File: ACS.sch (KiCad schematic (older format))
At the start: 30 parts, among them J1 5v? Igniter power source, J2 RJ45, J3 RJ45, P1 CONN_01X02, P10 ABT TOG, P11 LOX MPV, P12 LNCH SFT, P13 LNCH TOG, P14 CH4 MPV, P15 LOX VNT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

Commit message: Added version number
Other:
- note added: "Version: 4.10.18"
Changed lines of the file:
@@
 LIBS:power
 LIBS:device
+LIBS:switches
+LIBS:relays
+LIBS:motors
 LIBS:transistors
 LIBS:conn
@@
 	1750 3700 1750 5500
 NoConn ~ 1600 3550
+Text Notes 4550 5750 0    60   ~ 0
+Version: 4.10.18
 $EndSCHEMATC

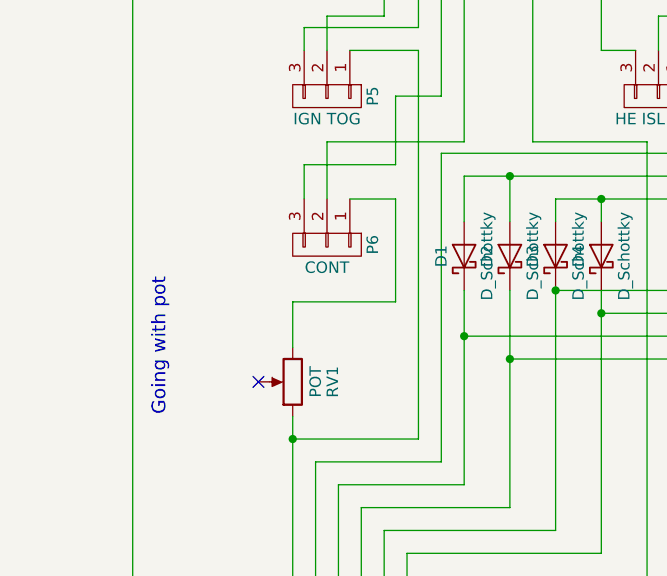
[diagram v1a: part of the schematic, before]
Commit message: Trimmer Resistor, finished circuit
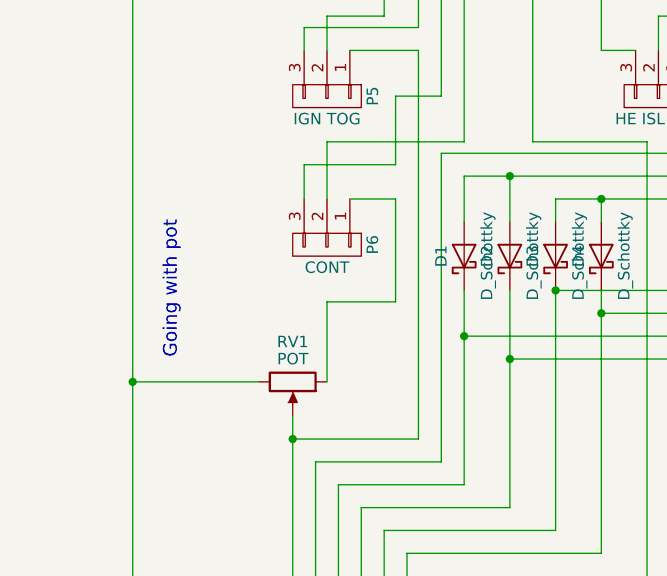
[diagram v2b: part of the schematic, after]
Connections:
- net at J2.1, P1.2 (P2), P10.3 (P3)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: now also RV1.3
- net at J2.8, P5.1 (P1): now also RV1.2; no longer RV1.1
- net at P6.1 (P1): now also RV1.1; no longer RV1.3
- no-connect marks 5 -> 4
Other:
- moved on the sheet: RV1
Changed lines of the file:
@@
 	3250 1300 3250 1500
-Wire Wire Line
-	2200 3200 1750 3200
 Wire Wire Line
 	2200 2750 2200 3200
 Wire Wire Line
-	2000 2750 2200 2750
+	2200 2750 2000 2750
 Wire Wire Line
 	2300 3800 1750 3800
@@
 NoConn ~ 1550 6300
 NoConn ~ 1300 4500
-Text Notes 1200 3700 1    60   ~ 0
+Text Notes 1250 3450 1    60   ~ 0
 Going with pot\n
 $Comp
@@
 F 3 "" H 1750 3550 50  0001 C CNN
 	1    1750 3550
-	-1   0    0    1
+	0    1    1    0
 $EndComp
 Wire Wire Line
-	1750 3200 1750 3400
-Wire Wire Line
 	1750 3700 1750 5500
-NoConn ~ 1600 3550
 Text Notes 4550 5750 0    60   ~ 0
 Version: 4.10.18
+Wire Wire Line
+	1900 3550 1900 3200
+Wire Wire Line
+	1900 3200 2200 3200
+Wire Wire Line
+	1600 3550 1050 3550
+Connection ~ 1050 3550
 $EndSCHEMATC

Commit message: Finished traces, and edge border
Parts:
- RV1: footprint (none) -> Potentiometers:Potentiometer_Trimmer_Vishay_T73XW_Vertical
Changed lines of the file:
@@
 F 0 "RV1" V 1575 3550 50  0000 C CNN
 F 1 "POT" V 1650 3550 50  0000 C CNN
-F 2 "" H 1750 3550 50  0001 C CNN
+F 2 "Potentiometers:Potentiometer_Trimmer_Vishay_T73XW_Vertical" H 1750 3550 50  0001 C CNN
 F 3 "" H 1750 3550 50  0001 C CNN
 	1    1750 3550
